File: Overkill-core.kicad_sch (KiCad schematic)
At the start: 16 parts, among them J1 USB_C_Receptacle_USB2.0_14P, J2 USB_C_Receptacle_USB2.0_14P, U1 CH343P, U12 CH334F, U2 HS28QI084RX, U3 ESP32-S3-WROOM-1U

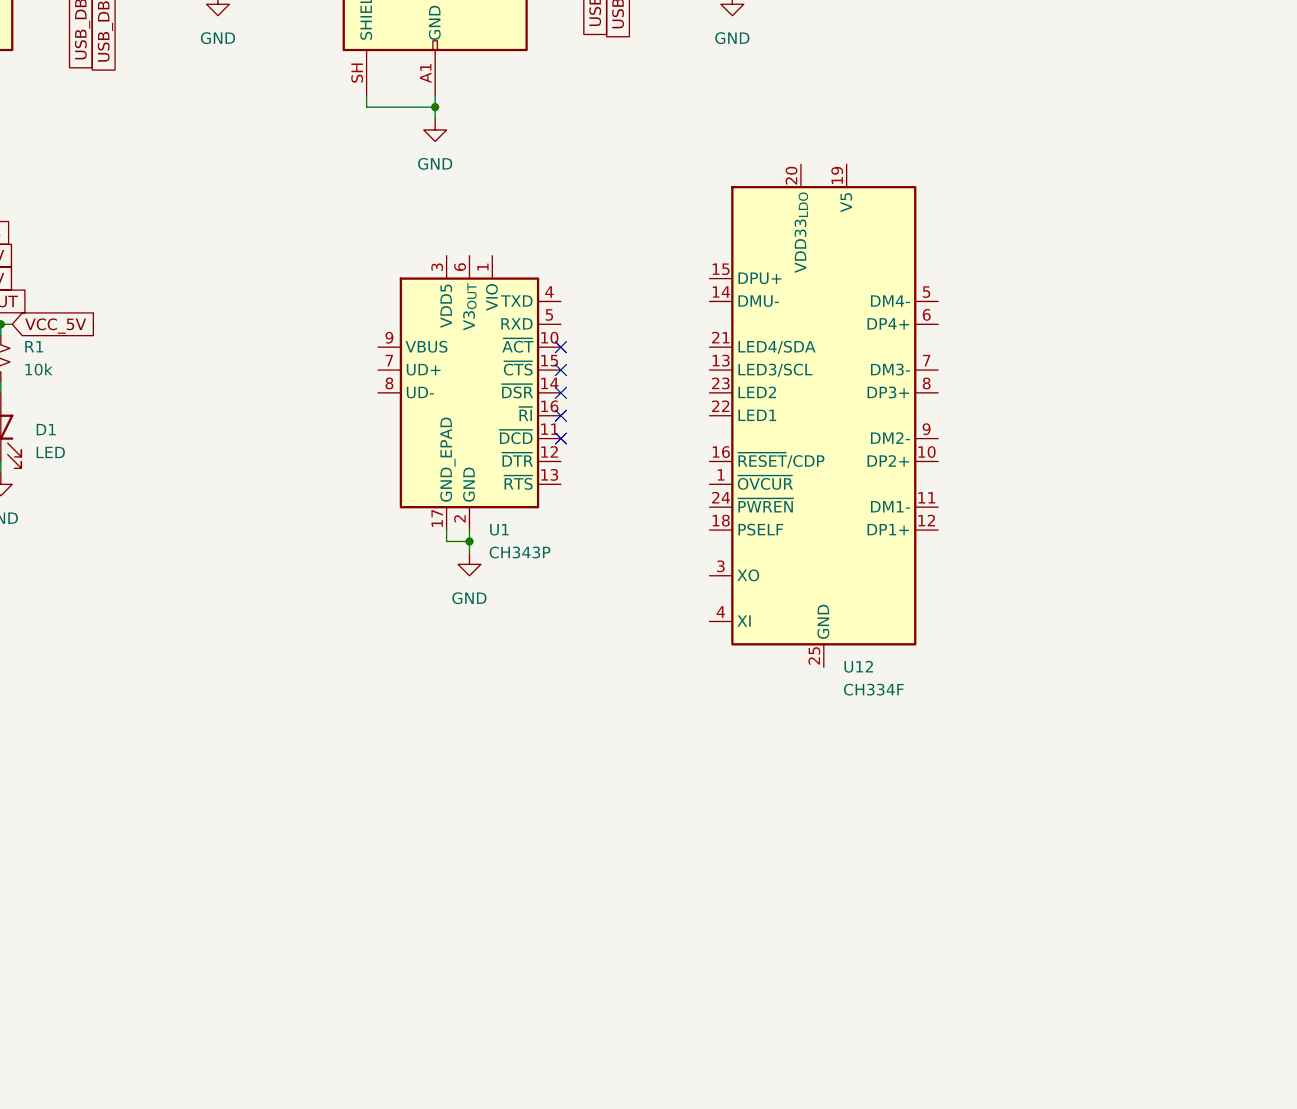
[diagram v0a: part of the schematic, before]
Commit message: route chips
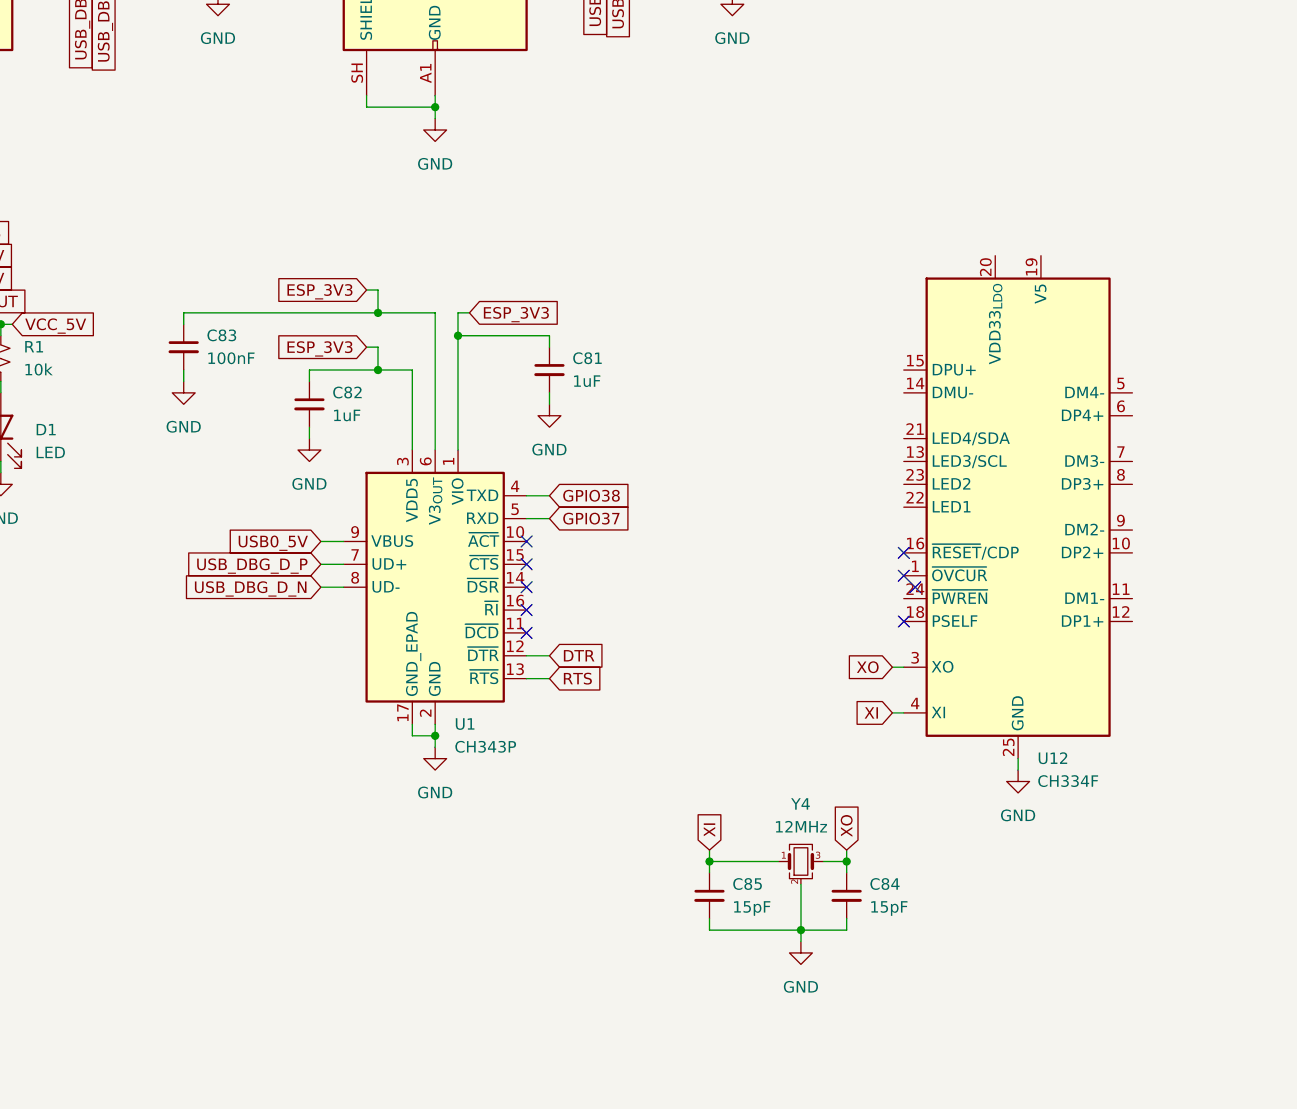
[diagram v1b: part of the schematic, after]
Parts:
- added C81, C82: 1uF, symbol Device:C_Small
- added C83: 100nF, symbol Device:C_Small
- added C84, C85: 15pF, symbol Device:C_Small
- added Y4: 12MHz, symbol Device:Crystal_GND24_Small
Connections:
- net ESP_3V3: now also U1.1 (VIO), U1.3 (VDD5), U1.6 (V3_{OUT}), C81.1, C82.1, C83.1
- net GND: now also U12.25 (GND), C81.2, C82.2, C83.2, C84.2, C85.2, Y4.2 (G), Y4.4 (G)
- net GPIO37: now also U1.5 (RXD)
- net GPIO38: now also U1.4 (TXD)
- net USB0_5V: now also U1.9 (VBUS)
- net USB_DBG_D_N: now also U1.8 (UD-)
- net USB_DBG_D_P: now also U1.7 (UD+)
- net XO: now reaches U12.3 (XO)
- net XO: now also C84.1, Y4.3
- net XI: now reaches U12.4 (XI)
- net XI: now also C85.1, Y4.1
- net DTR: now reaches U1.12 (~{DTR})
- net RTS: now reaches U1.13 (~{RTS})
- no-connect marks 5 -> 9
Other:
- moved on the sheet: U1, U12

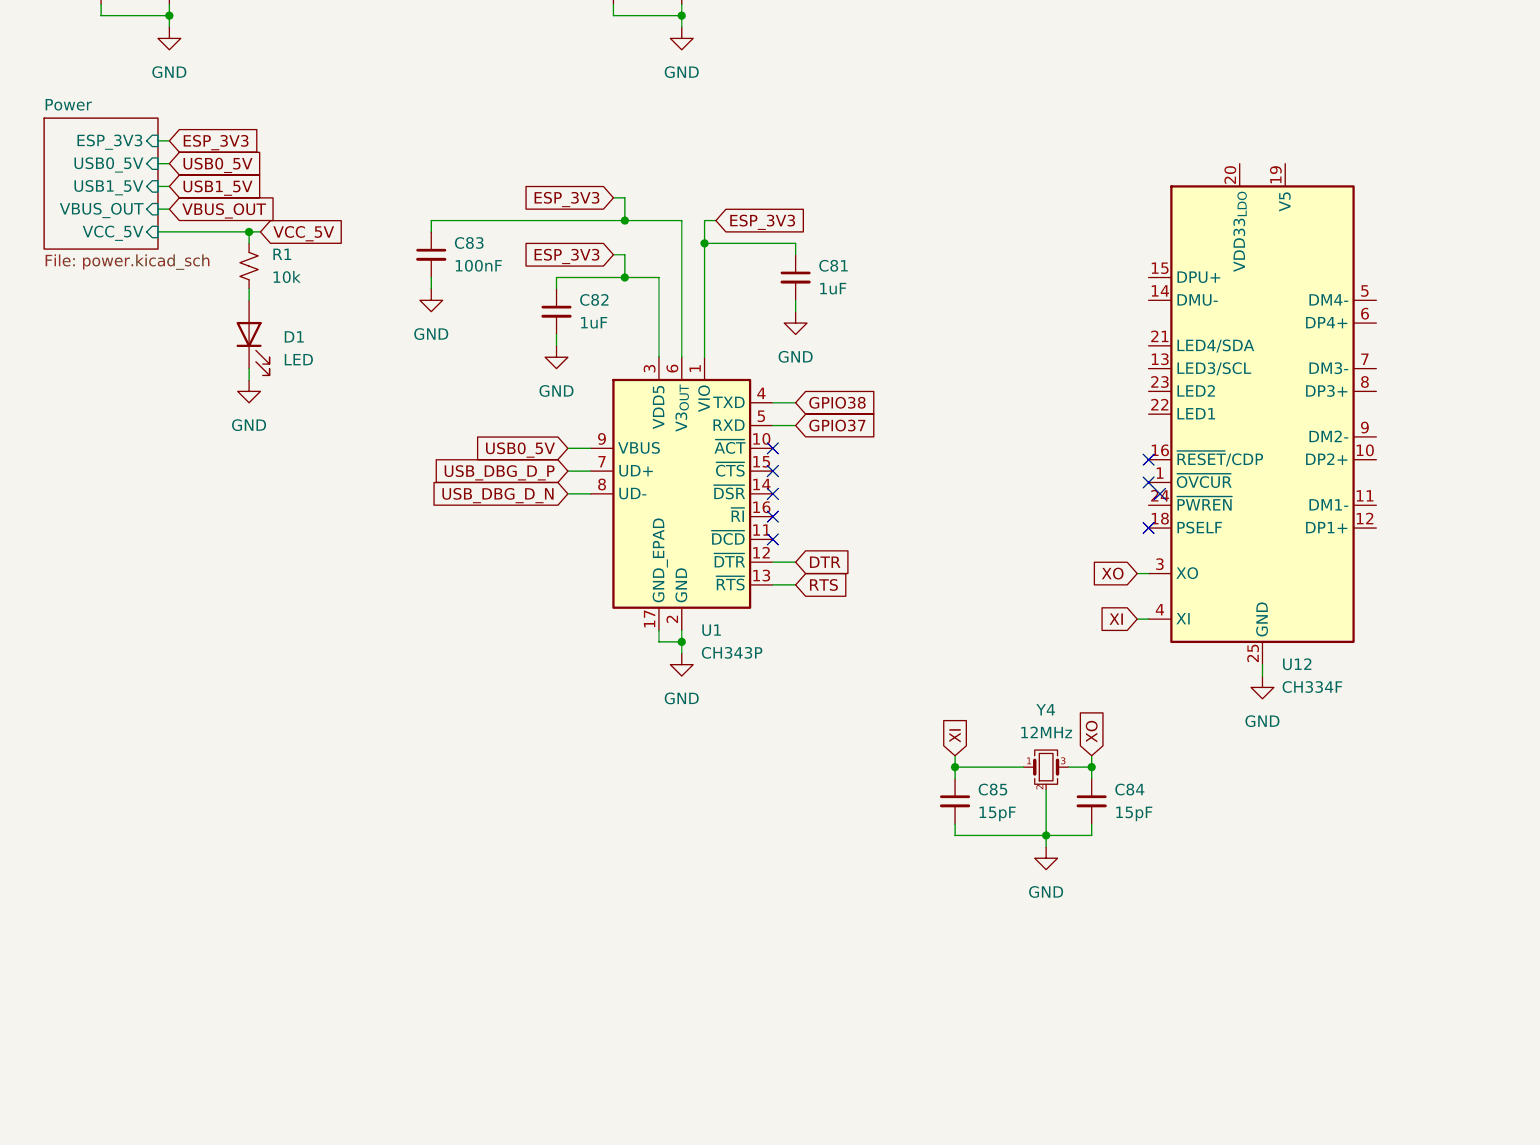
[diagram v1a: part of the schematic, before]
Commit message: add usb-uart circuitry
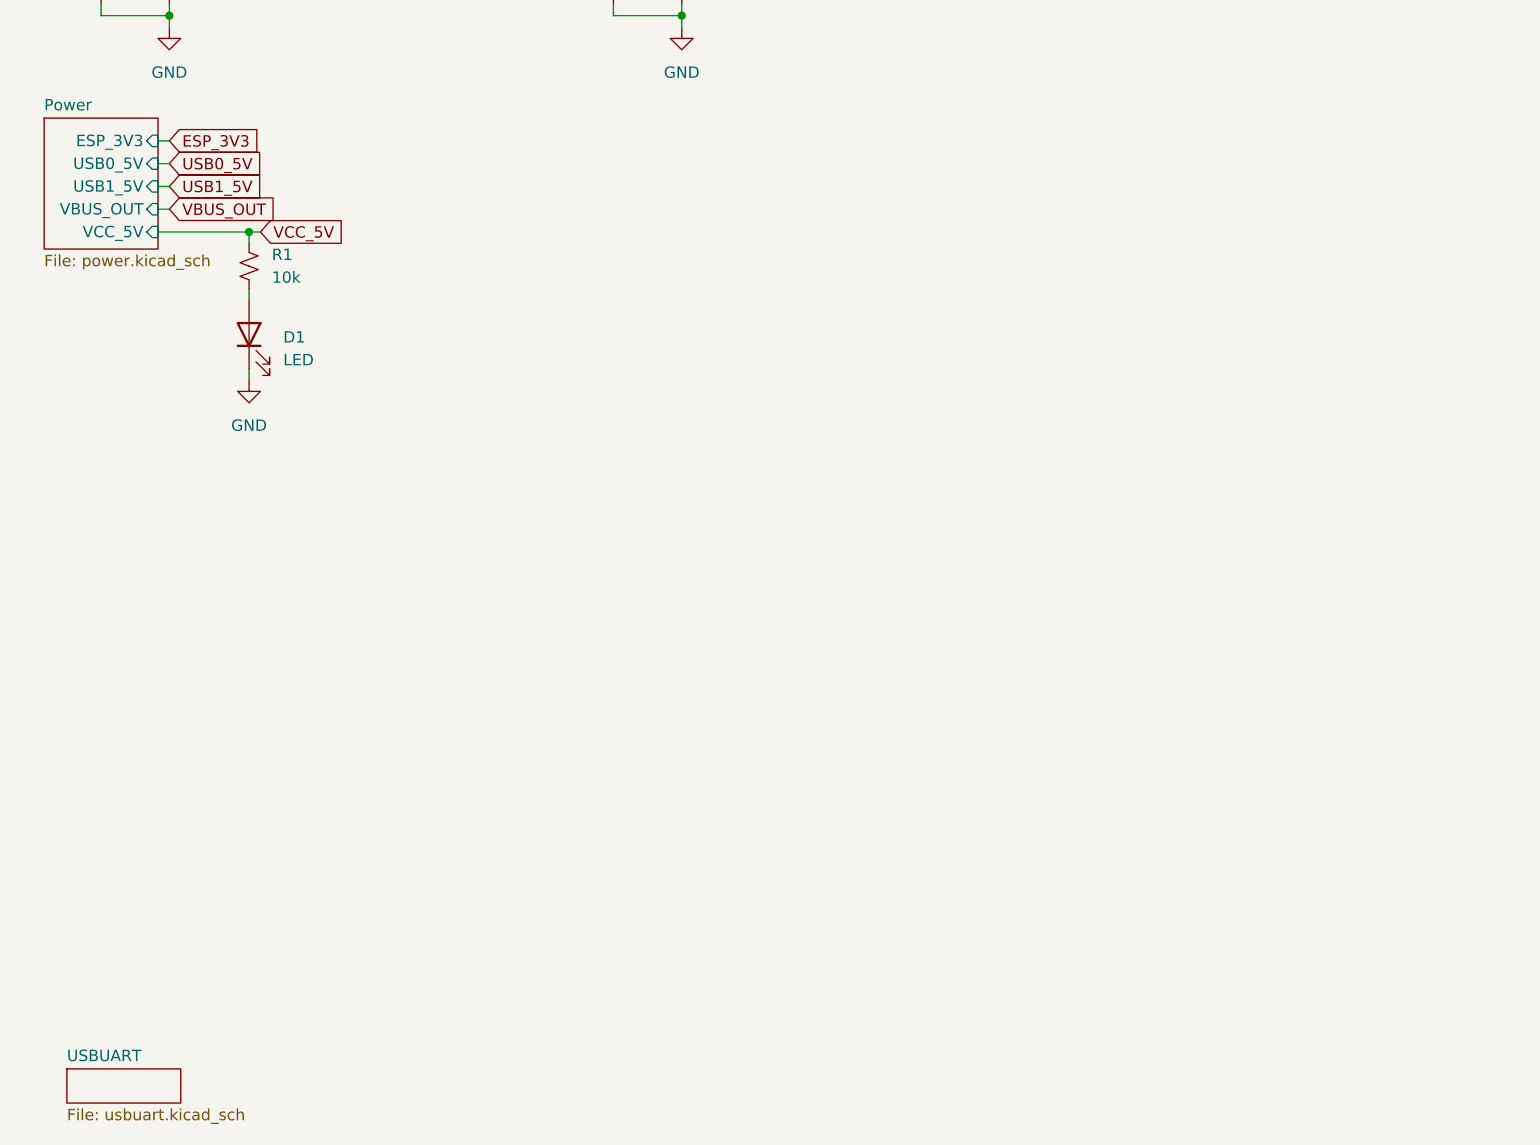
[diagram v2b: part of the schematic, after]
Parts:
- removed C81, C82: 1uF, symbol Device:C_Small
- removed C83: 100nF, symbol Device:C_Small
- removed C84, C85: 15pF, symbol Device:C_Small
- removed U1: CH343P, Package_DFN_QFN:WCH_QFN-16-1EP_3x3mm_P0.5mm_EP1.8x1.8mm, symbol Interface_USB:CH343P
- removed U12: CH334F, Package_DFN_QFN:QFN-24-1EP_4x4mm_P0.5mm_EP2.7x2.7mm, symbol Interface_USB:CH334F
- removed Y4: 12MHz, symbol Device:Crystal_GND24_Small
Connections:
- no-connect marks 9 -> 0
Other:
- added sheet USBUART (usbuart.kicad_sch)

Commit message: updates
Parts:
- removed D2, D3: SMF6V0A, Diode_SMD:D_SMF, symbol Diode:SMF6V0A
- removed J1, J2: USB_C_Receptacle_USB2.0_14P, symbol Connector:USB_C_Receptacle_USB2.0_14P
- removed R2, R3, R4, R5: 5.1k, symbol Device:R_Small_US
- renumbered U2 to U1, U3 to U2
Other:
- added sheet Interface (interface.kicad_sch)
- moved on the sheet: D1, R1
